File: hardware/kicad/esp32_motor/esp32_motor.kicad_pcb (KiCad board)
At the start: 2 copper layers, 120.3 x 42.5 mm, 121 parts, among them J201 Program, J401 MOTOR1, J402 MOTOR2, J403 MOTOR3, J404 MOTOR4, J501 24V_OUT, U1 BD62220AEFV, U2 BD62220AEFV, U3 ESP32-WROOM-32D, U401 74HC14, U402 74HC14, U501 TPS54302, U502 NCP1117-3.3_SOT223, U601 MPU-9250

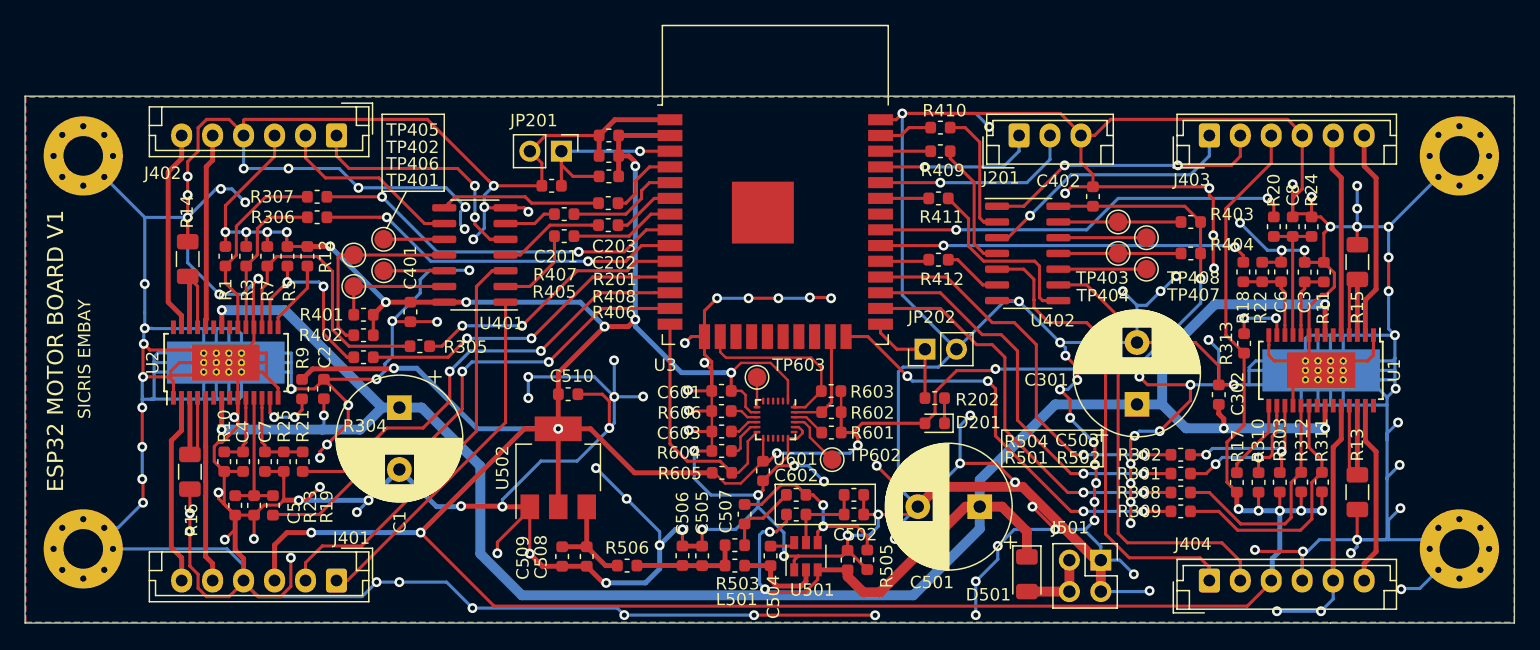
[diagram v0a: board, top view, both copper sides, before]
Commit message: Updated PCB Layout.  This is PCB release candidate 1
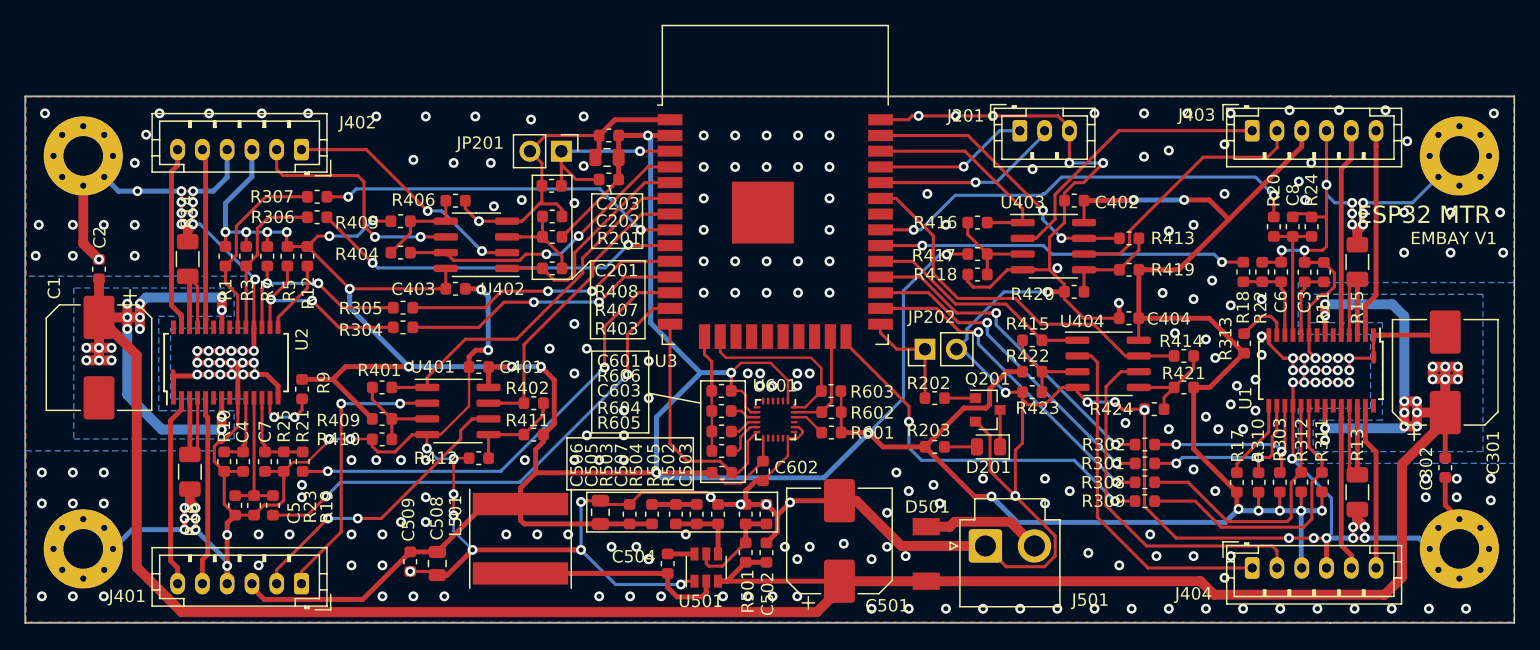
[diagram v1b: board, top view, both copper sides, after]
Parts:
- removed C510: 0.1uF, Capacitor_SMD:C_0603_1608Metric
- removed R506: 0R, Resistor_SMD:R_0603_1608Metric
- removed TP401, TP402, TP403, TP404, TP405, TP406, TP407, TP408, TP602, TP603: TP, TestPoint:TestPoint_Pad_D1.5mm
- removed U502: NCP1117-3.3_SOT223, Package_TO_SOT_SMD:SOT-223-3_TabPin2
- added C403: 0.1uF, Capacitor_SMD:C_0603_1608Metric, F.Cu at (83.4, 70.2)
- added C404: 0.1uF, Capacitor_SMD:C_0603_1608Metric, F.Cu at (137.8, 72.5)
- added Q201: MMBT2222, Package_TO_SOT_SMD:SOT-23, F.Cu at (126.4, 79.9)
- added R203: 220R, Resistor_SMD:R_0603_1608Metric, F.Cu at (122.1, 82.9)
- added R413: 50K, Resistor_SMD:R_0603_1608Metric, F.Cu at (137.8, 66.1)
- added R414: 50K, Resistor_SMD:R_0603_1608Metric, F.Cu at (142.2, 75.6)
- added R415: 50K, Resistor_SMD:R_0603_1608Metric, F.Cu at (130.0, 74.3)
- added R416: 50K, Resistor_SMD:R_0603_1608Metric, F.Cu at (125.6, 64.8)
- added R417: 10K, Resistor_SMD:R_0603_1608Metric, F.Cu at (125.6, 67.4)
- added R418: 10K, Resistor_SMD:R_0603_1608Metric, F.Cu at (125.6, 69.0)
- added R419: 10K, Resistor_SMD:R_0603_1608Metric, F.Cu at (137.8, 68.6)
- added R420: 10K, Resistor_SMD:R_0603_1608Metric, F.Cu at (133.4, 70.4)
- added R421: 10K, Resistor_SMD:R_0603_1608Metric, F.Cu at (142.2, 78.1)
- added R422: 10K, Resistor_SMD:R_0603_1608Metric, F.Cu at (130.0, 76.9)
- added R423: 10K, Resistor_SMD:R_0603_1608Metric, F.Cu at (130.0, 78.5)
- added R424: 10K, Resistor_SMD:R_0603_1608Metric, F.Cu at (139.8, 79.9)
- added U403: LM393, Package_SO:SOIC-8_3.9x4.9mm_P1.27mm, F.Cu at (131.7, 66.7)
- added U404: LM393, Package_SO:SOIC-8_3.9x4.9mm_P1.27mm, F.Cu at (136.1, 76.2)
- C1, C301, C501: footprint Capacitor_THT:CP_Radial_D10.0mm_P5.00mm -> Capacitor_SMD:CP_Elec_8x10
- C202, C506: footprint Capacitor_SMD:C_0603_1608Metric -> Capacitor_SMD:C_0805_2012Metric
- C508: value 10uF -> 22uF; footprint Capacitor_SMD:C_0603_1608Metric -> Capacitor_SMD:C_0805_2012Metric
- D201: footprint LED_SMD:LED_0603_1608Metric -> LED_SMD:LED_0805_2012Metric
- D501: footprint Diode_SMD:D_1206_3216Metric -> esp32_motor:SOD-128
- J201: footprint Connector_JST:JST_EH_B3B-EH-A_1x03_P2.50mm_Vertical -> Connector_JST:JST_PH_B3B-PH-K_1x03_P2.00mm_Vertical
- J401, J402, J403, J404: footprint Connector_JST:JST_EH_B6B-EH-A_1x06_P2.50mm_Vertical -> Connector_JST:JST_PH_B6B-PH-K_1x06_P2.00mm_Vertical
- J501: value 24V_OUT -> 24V_IN; footprint Connector_PinHeader_2.54mm:PinHeader_2x02_P2.54mm_Vertical -> Connector_JST:JST_VH_B2P-VH-B_1x02_P3.96mm_Vertical
- L501: footprint Inductor_SMD:L_0603_1608Metric -> Inductor_SMD:L_Taiyo-Yuden_NR-80xx
- R202: value R -> 10K
- R401, R402, R403, R404: value 10K -> 50K
- R405, R406, R407, R408, R409, R410, R411, R412: value 200R -> 10K
- R505: value 13.3K -> 22K
- U1, U2: footprint esp32_motor:HTSSOP-B28 -> esp32_motor:HTSSOP-28-BD62220AEFV
- U401, U402: value 74HC14 -> LM393; footprint Package_SO:SOIC-14_3.9x8.7mm_P1.27mm -> Package_SO:SOIC-8_3.9x4.9mm_P1.27mm
- moved R404 63.8 mm to (79.0, 67.2), turned to 0 degrees
- moved R403 51.7 mm to (91.2, 68.5)
- moved R410 51.6 mm to (77.5, 82.3), turned to 0 degrees
- moved R409 50.0 mm to (77.5, 80.7), turned to 0 degrees
- moved U402 44.5 mm to (85.1, 66.6), turned to 180 degrees
- moved R412 40.4 mm to (85.3, 83.8), turned to 0 degrees
- moved R411 37.8 mm to (89.7, 81.9)
- moved C301 25.0 mm to (163.3, 76.9)
- moved C1 24.6 mm to (54.6, 75.7)
- moved C2 20.6 mm to (54.6, 68.6)
- moved C302 19.2 mm to (163.3, 84.6), turned to 270 degrees
- moved L501 17.4 mm to (88.6, 90.4), turned to 90 degrees
- moved R402 14.8 mm to (89.7, 79.4)
- moved R405 13.3 mm to (79.0, 64.7)
- moved U401 12.7 mm to (83.6, 80.0), turned to 0 degrees
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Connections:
- net POWER_SAVE renamed Net-(R9-Pad2)
- C505 pad 2: 5V_OUT -> 3V3_OUT
- C506 pad 2: 5V_OUT -> 3V3_OUT
- C508 pad 2: Net-(C508-Pad2) -> 3V3_OUT
- C509 pad 2: Net-(C508-Pad2) -> 3V3_OUT
- D201 pad 2: 3V3_OUT -> Net-(D201-Pad2)
- J501 pad 2: GND -> Net-(D501-Pad2)
- L501 pad 2: 5V_OUT -> 3V3_OUT
- R202 pad 1: Net-(D201-Pad1) -> Net-(Q201-Pad1)
- R401 pad 1: 3V3_OUT -> Net-(R401-Pad1)
- R401 pad 2: Net-(R401-Pad2) -> MOT1_ENCA
- R402 pad 1: 3V3_OUT -> Net-(R402-Pad1)
- R402 pad 2: Net-(R402-Pad2) -> MOT1_ENCB
- R403 pad 1: 3V3_OUT -> Net-(R403-Pad1)
- R403 pad 2: Net-(R403-Pad2) -> MOT2_ENCA
- R404 pad 1: 3V3_OUT -> Net-(R404-Pad1)
- R404 pad 2: Net-(R404-Pad2) -> MOT2_ENCB
- R405 pad 1: Net-(R405-Pad1) -> 3V3_OUT
- R405 pad 2: MOT1_ENCA -> Net-(R404-Pad1)
- R406 pad 1: Net-(R406-Pad1) -> GND
- R406 pad 2: MOT1_ENCB -> Net-(R404-Pad1)
- R407 pad 1: Net-(R407-Pad1) -> 3V3_OUT
- R407 pad 2: MOT2_ENCA -> Net-(R403-Pad1)
- R408 pad 1: Net-(R408-Pad1) -> GND
- R408 pad 2: MOT2_ENCB -> Net-(R403-Pad1)
- R409 pad 1: Net-(R409-Pad1) -> 3V3_OUT
- R409 pad 2: MOT3_ENCA -> Net-(R401-Pad1)
- R410 pad 1: Net-(R410-Pad1) -> GND
- R410 pad 2: MOT3_ENCB -> Net-(R401-Pad1)
- R411 pad 1: Net-(R411-Pad1) -> 3V3_OUT
- R411 pad 2: MOT4_ENCB -> Net-(R402-Pad1)
- R412 pad 1: Net-(R412-Pad1) -> GND
- R412 pad 2: MOT4_ENCA -> Net-(R402-Pad1)
- R503 pad 1: 5V_OUT -> 3V3_OUT
- U3 pad 6: MOT1_ENCB -> MOT1_ENCA
- U3 pad 7: MOT1_ENCA -> MOT1_ENCB
- U401 pad 1: Net-(J401-Pad1) -> MOT1_ENCA
- U401 pad 2: Net-(R405-Pad1) -> Net-(J401-Pad1)
- U401 pad 3: Net-(J401-Pad2) -> Net-(R401-Pad1)
- U401 pad 4: Net-(R406-Pad1) -> GND
- U401 pad 5: Net-(J402-Pad1) -> Net-(R402-Pad1)
- U401 pad 6: Net-(R407-Pad1) -> Net-(J401-Pad2)
- U401 pad 7: GND -> MOT1_ENCB
- U401 pad 8: Net-(R408-Pad1) -> 3V3_OUT
- U402 pad 1: Net-(J403-Pad2) -> MOT2_ENCA
- U402 pad 2: Net-(R410-Pad1) -> Net-(J402-Pad1)
- U402 pad 3: Net-(J403-Pad1) -> Net-(R403-Pad1)
- U402 pad 4: Net-(R409-Pad1) -> GND
- U402 pad 5: Net-(J404-Pad1) -> Net-(R404-Pad1)
- U402 pad 6: Net-(R412-Pad1) -> Net-(J402-Pad2)
- U402 pad 7: GND -> MOT2_ENCB
- U402 pad 8: Net-(R411-Pad1) -> 3V3_OUT
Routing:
- net GND: track 1037.4 -> 529.0 mm, vias 147 -> 310
- net 24VDC: track 194.7 -> 248.1 mm, vias 8 -> 32
- net MOT4_ENCB: track 3.89 -> 30.8 mm
- net MOT1_ENCA: track 8.49 -> 31.0 mm
- net MOT1_ENCB: track 5.09 -> 24.4 mm
- net MOT3_ENCB: track 4.31 -> 23.2 mm, vias 0 -> 2
- net MOT2_ENCB: track 6.01 -> 24.3 mm, vias 0 -> 2
- net Net-(R402-Pad2): track 15.8 -> 0.00 mm
- net Net-(R411-Pad1): track 15.1 -> 0.00 mm
- net MOT4_ENCA: track 3.95 -> 18.5 mm
- net MOT3_ENCA: track 4.05 -> 17.4 mm
- net Net-(R408-Pad1): track 13.0 -> 0.00 mm
- net Net-(R410-Pad1): track 10.5 -> 0.00 mm
- net Net-(J401-Pad2): track 34.2 -> 23.7 mm, vias 0 -> 2
- net Net-(R409-Pad1): track 10.5 -> 0.00 mm
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- added copper zone on B.Cu, net 24VDC
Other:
- board text added: "EMBAY V1"
- board text added: "ESP32 MTR"
- board text removed: "ESP32 MOTOR BOARD V1"
- board text removed: "SICRIS EMBAY"

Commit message: PCB Release v1
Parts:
- removed Q201: MMBT2222, Package_TO_SOT_SMD:SOT-23
- removed R202: 10K, Resistor_SMD:R_0603_1608Metric
- moved D201 5.86 mm to (122.2, 78.8), turned to 0 degrees
- moved R203 1.70 mm to (122.4, 81.3)
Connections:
- JP202 pad 1: Net-(JP202-Pad1) -> Net-(D201-Pad1)
- U3 pad 13: MOT1_VREF -> MPU_9250_INT
- U3 pad 14: MPU_9250_INT -> MOT1_VREF
- U3 pad 24: MOT4_INB -> MOT4_VREF
- U3 pad 25: Net-(JP202-Pad1) -> Net-(D201-Pad1)
- U3 pad 28: MOT3_INB -> MOT4_ENCA
- U3 pad 29: MOT4_ENCA -> MOT3_INB
- U3 pad 30: MOT4_VREF -> MOT4_INB
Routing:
- net Net-(JP202-Pad1): track 8.79 -> 0.00 mm
- net MOT4_INB: track 31.1 -> 38.6 mm
- net MOT4_VREF: track 29.9 -> 36.7 mm
- net GND: track 529.0 -> 522.1 mm, vias 310 -> 309
- net Net-(D201-Pad1): track 2.99 -> 8.87 mm, vias 0 -> 1
- net MPU_9250_INT: track 20.1 -> 24.1 mm
- net Net-(Q201-Pad1): track 2.49 -> 0.00 mm
- net Net-(C504-Pad1): track 17.5 -> 16.1 mm
- net MOT3_INB: track 26.7 -> 27.9 mm, vias 2 -> 4
- net MOT4_ENCA: track 18.5 -> 18.0 mm
- net MOT1_VREF: track 40.9 -> 40.4 mm
- net 3V3_OUT: track 378.2 -> 377.8 mm, vias 23 -> 24
- added copper zone on F.Cu, net 24VDC
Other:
- board text added: "ESP32 MOTOR BOARD V1"
- board text added: "ZPL HACK PROJECT"
